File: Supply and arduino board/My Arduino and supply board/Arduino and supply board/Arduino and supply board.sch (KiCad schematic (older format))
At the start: 62 parts, among them J1 USB_C_Receptacle_USB2.0, J2 Conn_01x03, J3 Conn_01x03, J4 Conn_01x03, J5 Conn_01x03, J6 Conn_01x03, J7 Conn_01x03, Q2 16MHz, T1 FDN340V, U1 LM358D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

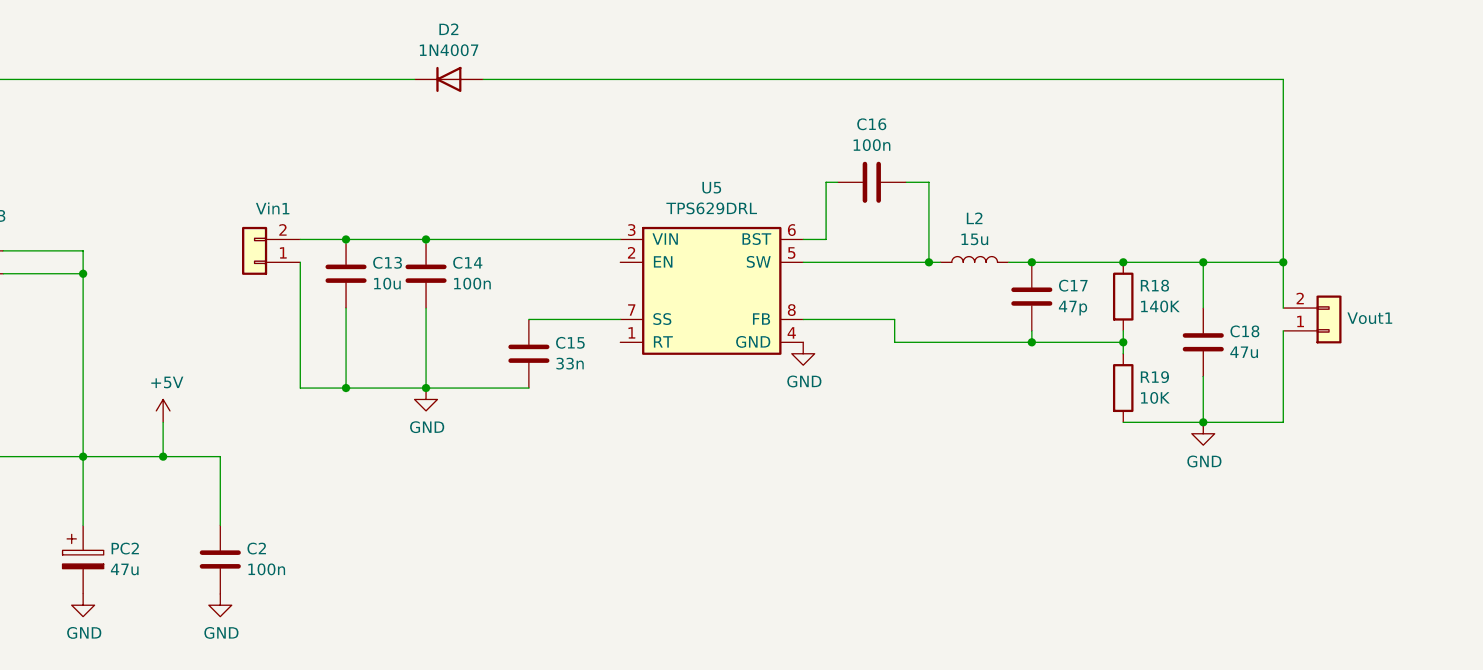
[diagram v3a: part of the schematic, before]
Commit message: new DC-DC power supply
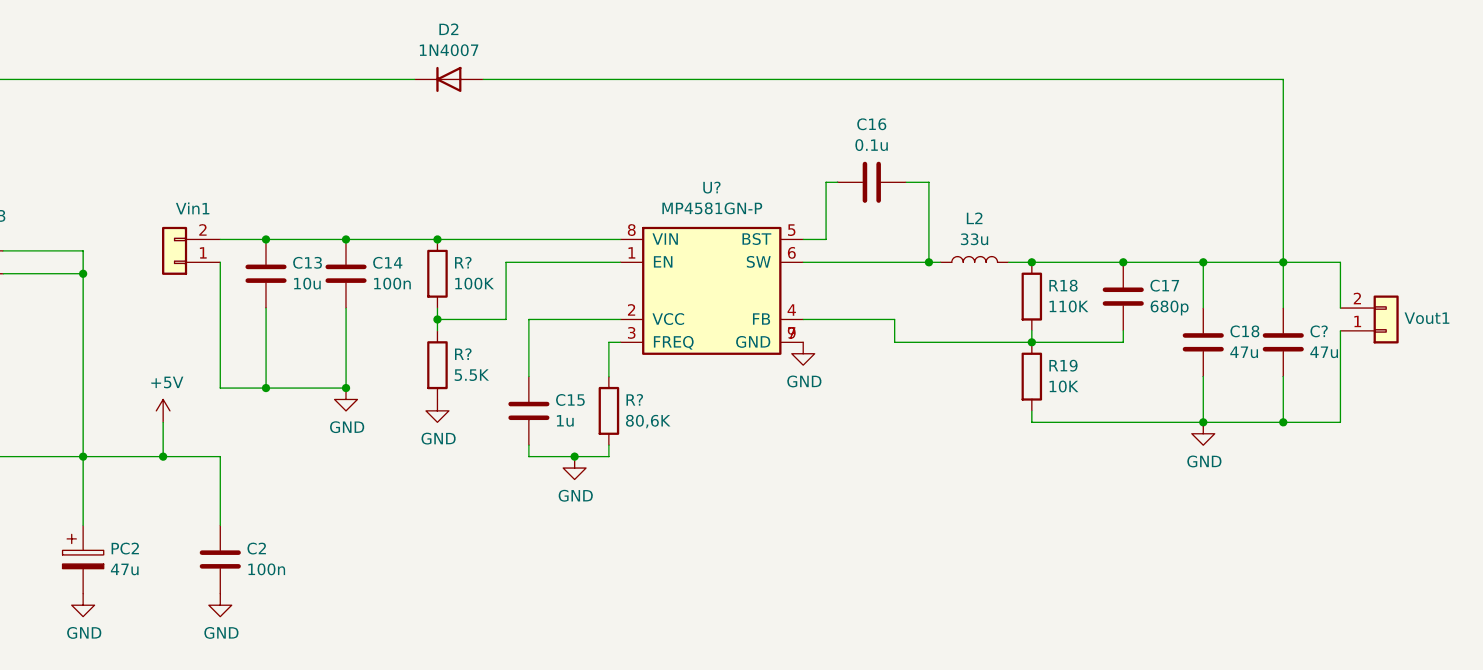
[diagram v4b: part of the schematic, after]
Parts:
- removed U5: TPS629DRL, Package_TO_SOT_SMD:TSOT-23-8, symbol Assembly_board_schem:TPS629DRL
- added C?: 47u, Capacitor_SMD:C_0603_1608Metric, symbol Device:C
- added R?: 100K, Resistor_SMD:R_0402_1005Metric, symbol Device:R
- added R?: 5.5K, Resistor_SMD:R_0402_1005Metric, symbol Device:R
- added R?: 80,6K, Resistor_SMD:R_0402_1005Metric, symbol Device:R
- added U?: MP4581GN-P, Package_SO:SOIC-8-1EP_3.9x4.9mm_P1.27mm_EP2.514x3.2mm, symbol Assembly_board_schem:MP4581GN-P
- C15: value 33n -> 1u
- C16: value 100n -> 0.1u
- C17: value 47p -> 680p
- L2: value 15u -> 33u
- R18: value 140K -> 110K
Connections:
- net GND: now also C?.1, R?.2, R?.2, U?.7 (GND), U?.9 (GND)
- net at C15.1: now also U?.2 (VCC)
- net at C13.1, C14.1, Vin1.2 (Pin_2): now also R?.1, U?.8 (VIN)
- net at C16.1, L2.1: now also U?.6 (SW)
- net at C16.2: now also U?.5 (BST)
- net at C17.1, R18.2, R19.1: now also U?.4 (FB)
- net at C17.2, C18.2, D2.2 (A)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: now also C?.2
- new net: R?.1, R?.2, U?.1 (EN)
- new net: R?.1, U?.3 (FREQ)
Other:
- moved on the sheet: C13, C14, C15, C17, R18, R19, Vin1, Vout1
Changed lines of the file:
@@
 L Device:C C15
 U 1 1 65724CD8
-P 12200 1850
-F 0 "C15" H 12315 1896 50  0000 L CNN
-F 1 "33n" H 12315 1805 50  0000 L CNN
-F 2 "Capacitor_SMD:C_0603_1608Metric" H 12238 1700 50  0001 C CNN
-F 3 "~" H 12200 1850 50  0001 C CNN
-	1    12200 1850
+P 12200 2100
+F 0 "C15" H 12315 2146 50  0000 L CNN
+F 1 "1u" H 12315 2055 50  0000 L CNN
+F 2 "Capacitor_SMD:C_0603_1608Metric" H 12238 1950 50  0001 C CNN
+F 3 "~" H 12200 2100 50  0001 C CNN
+	1    12200 2100
 	1    0    0    -1
 $EndComp
@@
 L Device:C C14
 U 1 1 6572633A
-P 11750 1500
-F 0 "C14" H 11865 1546 50  0000 L CNN
-F 1 "100n" H 11865 1455 50  0000 L CNN
-F 2 "Capacitor_SMD:C_0603_1608Metric" H 11788 1350 50  0001 C CNN
-F 3 "~" H 11750 1500 50  0001 C CNN
-	1    11750 1500
-	1    0    0    -1
-$EndComp
-$Comp
-L Device:C C13
-U 1 1 6572672D
 P 11400 1500
-F 0 "C13" H 11515 1546 50  0000 L CNN
-F 1 "10u" H 11515 1455 50  0000 L CNN
+F 0 "C14" H 11515 1546 50  0000 L CNN
+F 1 "100n" H 11515 1455 50  0000 L CNN
 F 2 "Capacitor_SMD:C_0603_1608Metric" H 11438 1350 50  0001 C CNN
 F 3 "~" H 11400 1500 50  0001 C CNN
@@
 $EndComp
 $Comp
+L Device:C C13
+U 1 1 6572672D
+P 11050 1500
+F 0 "C13" H 11165 1546 50  0000 L CNN
+F 1 "10u" H 11165 1455 50  0000 L CNN
+F 2 "Capacitor_SMD:C_0603_1608Metric" H 11088 1350 50  0001 C CNN
+F 3 "~" H 11050 1500 50  0001 C CNN
+	1    11050 1500
+	1    0    0    -1
+$EndComp
+$Comp
 L Connector_Generic:Conn_01x02 Vin1
 U 1 1 657270CA
-P 11000 1450
-F 0 "Vin1" H 10918 1217 50  0000 C CNN
-F 1 "Conn_01x02" H 10918 1216 50  0001 C CNN
-F 2 "Connector_PinSocket_2.54mm:PinSocket_1x02_P2.54mm_Horizontal" H 11000 1450 50  0001 C CNN
-F 3 "~" H 11000 1450 50  0001 C CNN
-	1    11000 1450
+P 10650 1450
+F 0 "Vin1" H 10568 1217 50  0000 C CNN
+F 1 "Conn_01x02" H 10568 1216 50  0001 C CNN
+F 2 "Connector_PinSocket_2.54mm:PinSocket_1x02_P2.54mm_Horizontal" H 10650 1450 50  0001 C CNN
+F 3 "~" H 10650 1450 50  0001 C CNN
+	1    10650 1450
 	-1   0    0    1
 $EndComp
@@
 P 13700 1100
 F 0 "C16" V 13448 1100 50  0000 C CNN
-F 1 "100n" V 13539 1100 50  0000 C CNN
+F 1 "0.1u" V 13539 1100 50  0000 C CNN
 F 2 "Capacitor_SMD:C_0603_1608Metric" H 13738 950 50  0001 C CNN
 F 3 "~" H 13700 1100 50  0001 C CNN
@@
 L Device:C C17
 U 1 1 657293B3
-P 14400 1600
-F 0 "C17" H 14285 1554 50  0000 R CNN
-F 1 "47p" H 14285 1645 50  0000 R CNN
-F 2 "Capacitor_SMD:C_0603_1608Metric" H 14438 1450 50  0001 C CNN
-F 3 "~" H 14400 1600 50  0001 C CNN
-	1    14400 1600
+P 14800 1600
+F 0 "C17" H 14685 1554 50  0000 R CNN
+F 1 "680p" H 14685 1645 50  0000 R CNN
+F 2 "Capacitor_SMD:C_0603_1608Metric" H 14838 1450 50  0001 C CNN
+F 3 "~" H 14800 1600 50  0001 C CNN
+	1    14800 1600
 	-1   0    0    1
 $EndComp
@@
 L Connector_Generic:Conn_01x02 Vout1
 U 1 1 65781F86
-P 15700 1750
-F 0 "Vout1" H 15780 1696 50  0000 L CNN
-F 1 "Conn_01x02" H 15780 1651 50  0001 L CNN
-F 2 "Connector_PinSocket_2.54mm:PinSocket_1x02_P2.54mm_Horizontal" H 15700 1750 50  0001 C CNN
-F 3 "~" H 15700 1750 50  0001 C CNN
-	1    15700 1750
+P 15950 1750
+F 0 "Vout1" H 16030 1696 50  0000 L CNN
+F 1 "Conn_01x02" H 16030 1651 50  0001 L CNN
+F 2 "Connector_PinSocket_2.54mm:PinSocket_1x02_P2.54mm_Horizontal" H 15950 1750 50  0001 C CNN
+F 3 "~" H 15950 1750 50  0001 C CNN
+	1    15950 1750
 	1    0    0    1
 $EndComp
 Wire Wire Line
-	11200 1350 11400 1350
+	10850 1350 11050 1350
+Connection ~ 11050 1350
+Wire Wire Line
+	11050 1350 11400 1350
 Connection ~ 11400 1350
 Wire Wire Line
-	11400 1350 11750 1350
-Connection ~ 11750 1350
-Wire Wire Line
-	11750 1350 12600 1350
-Wire Wire Line
-	11200 1450 11200 2000
-Wire Wire Line
-	11200 2000 11400 2000
-Wire Wire Line
-	12200 1700 12600 1700
-Wire Wire Line
-	11750 1650 11750 2000
-Connection ~ 11750 2000
-Wire Wire Line
-	11750 2000 12200 2000
+	10850 1450 10850 2000
+Wire Wire Line
+	10850 2000 11050 2000
 Wire Wire Line
 	11400 1650 11400 2000
 Connection ~ 11400 2000
 Wire Wire Line
-	11400 2000 11750 2000
+	11050 1650 11050 2000
+Connection ~ 11050 2000
+Wire Wire Line
+	11050 2000 11400 2000
 $Comp
 L power:GND #PWR0137
 U 1 1 65881DF1
-P 11750 2000
-F 0 "#PWR0137" H 11750 1750 50  0001 C CNN
-F 1 "GND" H 11755 1827 50  0000 C CNN
-F 2 "" H 11750 2000 50  0001 C CNN
-F 3 "" H 11750 2000 50  0001 C CNN
-	1    11750 2000
+P 11400 2000
+F 0 "#PWR0137" H 11400 1750 50  0001 C CNN
+F 1 "GND" H 11405 1827 50  0000 C CNN
+F 2 "" H 11400 2000 50  0001 C CNN
+F 3 "" H 11400 2000 50  0001 C CNN
+	1    11400 2000
 	1    0    0    -1
 $EndComp
@@
 P 14150 1450
 F 0 "L2" V 14340 1450 50  0000 C CNN
-F 1 "15u" V 14249 1450 50  0000 C CNN
+F 1 "33u" V 14249 1450 50  0000 C CNN
 F 2 "Inductor_SMD:L_Taiyo-Yuden_MD-5050" H 14150 1450 50  0001 C CNN
 F 3 "~" H 14150 1450 50  0001 C CNN
@@
 L Device:R R18
 U 1 1 658844CA
-P 14800 1600
-F 0 "R18" H 14870 1646 50  0000 L CNN
-F 1 "140K" H 14870 1555 50  0000 L CNN
-F 2 "Resistor_SMD:R_0402_1005Metric" V 14730 1600 50  0001 C CNN
-F 3 "~" H 14800 1600 50  0001 C CNN
-	1    14800 1600
+P 14400 1600
+F 0 "R18" H 14470 1646 50  0000 L CNN
+F 1 "110K" H 14470 1555 50  0000 L CNN
+F 2 "Resistor_SMD:R_0402_1005Metric" V 14330 1600 50  0001 C CNN
+F 3 "~" H 14400 1600 50  0001 C CNN
+	1    14400 1600
 	1    0    0    -1
 $EndComp
@@
 L Device:R R19
 U 1 1 658858B2
-P 14800 2000
-F 0 "R19" H 14870 2046 50  0000 L CNN
-F 1 "10K" H 14870 1955 50  0000 L CNN
-F 2 "Resistor_SMD:R_0402_1005Metric" V 14730 2000 50  0001 C CNN
-F 3 "~" H 14800 2000 50  0001 C CNN
-	1    14800 2000
+P 14400 1950
+F 0 "R19" H 14470 1996 50  0000 L CNN
+F 1 "10K" H 14470 1905 50  0000 L CNN
+F 2 "Resistor_SMD:R_0402_1005Metric" V 14330 1950 50  0001 C CNN
+F 3 "~" H 14400 1950 50  0001 C CNN
+	1    14400 1950
 	1    0    0    -1
 $EndComp
@@
 Wire Wire Line
 	14800 1450 15150 1450
-Wire Wire Line
-	15500 1450 15500 1650
 Connection ~ 14800 1450
 Wire Wire Line
@@
 Connection ~ 15150 2150
 Wire Wire Line
-	15150 2150 14800 2150
-Wire Wire Line
-	14800 1850 14800 1800
-Wire Wire Line
 	14800 1800 14400 1800
 Wire Wire Line
@@
 Wire Wire Line
 	13800 1700 13400 1700
-Connection ~ 14800 1800
 Wire Wire Line
 	14800 1800 14800 1750
@@
 F 3 "" H 9600 1500 50  0001 C CNN
 	1    9600 1500
-	1    0    0    -1
-$EndComp
-$Comp
-L Assembly_board_schem:TPS629DRL U5
-U 1 1 657CF2BB
-P 13000 1550
-F 0 "U5" H 13000 1975 50  0000 C CNN
-F 1 "TPS629DRL" H 13000 1884 50  0000 C CNN
-F 2 "Package_TO_SOT_SMD:TSOT-23-8" H 13000 1550 50  0001 C CNN
-F 3 "" H 13000 1550 50  0001 C CNN
-	1    13000 1550
 	1    0    0    -1
 $EndComp
@@
 Wire Wire Line
 	15500 650  12000 650
-Connection ~ 15500 1450
 Wire Wire Line
 	11700 650  8600 650
@@
 Wire Wire Line
 	8600 2300 8850 2300
-Wire Wire Line
-	15500 1750 15500 2150
+$Comp
+L Assembly_board_schem:MP4581GN-P U?
+U 1 1 658409AE
+P 13000 1550
+F 0 "U?" H 13000 1975 50  0000 C CNN
+F 1 "MP4581GN-P" H 13000 1884 50  0000 C CNN
+F 2 "Package_SO:SOIC-8-1EP_3.9x4.9mm_P1.27mm_EP2.514x3.2mm" H 13000 1550 50  0001 C CNN
+F 3 "" H 13000 1550 50  0001 C CNN
+	1    13000 1550
+	1    0    0    -1
+$EndComp
+$Comp
+L Device:R R?
+U 1 1 6582C206
+P 11800 1500
+F 0 "R?" H 11870 1546 50  0000 L CNN
+F 1 "100K" H 11870 1455 50  0000 L CNN
+F 2 "Resistor_SMD:R_0402_1005Metric" V 11730 1500 50  0001 C CNN
+F 3 "~" H 11800 1500 50  0001 C CNN
+	1    11800 1500
+	1    0    0    -1
+$EndComp
+$Comp
+L Device:R R?
+U 1 1 6582CDAE
+P 11800 1900
+F 0 "R?" H 11870 1946 50  0000 L CNN
+F 1 "5.5K" H 11870 1855 50  0000 L CNN
+F 2 "Resistor_SMD:R_0402_1005Metric" V 11730 1900 50  0001 C CNN
+F 3 "~" H 11800 1900 50  0001 C CNN
+	1    11800 1900
+	1    0    0    -1
+$EndComp
+Wire Wire Line
+	12100 1700 11800 1700
+Wire Wire Line
+	11800 1700 11800 1650
+Wire Wire Line
+	11800 1750 11800 1700
+Connection ~ 11800 1700
+Wire Wire Line
+	14400 2100 14400 2150
+Wire Wire Line
+	14400 2150 15150 2150
+Wire Wire Line
+	11400 1350 11800 1350
+Connection ~ 11800 1350
+Wire Wire Line
+	11800 1350 12600 1350
+Wire Wire Line
+	12100 1450 12100 1700
+Wire Wire Line
+	12100 1450 12600 1450
+$Comp
+L power:GND #PWR?
+U 1 1 658C02C0
+P 11800 2050
+F 0 "#PWR?" H 11800 1800 50  0001 C CNN
+F 1 "GND" H 11805 1877 50  0000 C CNN
+F 2 "" H 11800 2050 50  0001 C CNN
+F 3 "" H 11800 2050 50  0001 C CNN
+	1    11800 2050
+	1    0    0    -1
+$EndComp
+$Comp
+L Device:R R?
+U 1 1 658C089B
+P 12550 2100
+F 0 "R?" H 12620 2146 50  0000 L CNN
+F 1 "80,6K" H 12620 2055 50  0000 L CNN
+F 2 "Resistor_SMD:R_0402_1005Metric" V 12480 2100 50  0001 C CNN
+F 3 "~" H 12550 2100 50  0001 C CNN
+	1    12550 2100
+	1    0    0    -1
+$EndComp
+Wire Wire Line
+	12600 1800 12550 1800
+Wire Wire Line
+	12550 1800 12550 1950
+Wire Wire Line
+	12600 1700 12200 1700
+Wire Wire Line
+	12200 1700 12200 1950
+Wire Wire Line
+	12200 2250 12200 2300
+Wire Wire Line
+	12200 2300 12400 2300
+Wire Wire Line
+	12550 2300 12550 2250
+$Comp
+L power:GND #PWR?
+U 1 1 658FFE1C
+P 12400 2300
+F 0 "#PWR?" H 12400 2050 50  0001 C CNN
+F 1 "GND" H 12405 2127 50  0000 C CNN
+F 2 "" H 12400 2300 50  0001 C CNN
+F 3 "" H 12400 2300 50  0001 C CNN
+	1    12400 2300
+	1    0    0    -1
+$EndComp
+Connection ~ 12400 2300
+Wire Wire Line
+	12400 2300 12550 2300
+$Comp
+L Device:C C?
+U 1 1 659008EC
+P 15500 1800
+F 0 "C?" H 15385 1754 50  0000 R CNN
+F 1 "47u" H 15385 1845 50  0000 R CNN
+F 2 "Capacitor_SMD:C_0603_1608Metric" H 15538 1650 50  0001 C CNN
+F 3 "~" H 15500 1800 50  0001 C CNN
+	1    15500 1800
+	-1   0    0    1
+$EndComp
+Wire Wire Line
+	15500 1450 15500 1650
+Connection ~ 15500 1450
+Wire Wire Line
+	15500 1950 15500 2150
+Wire Wire Line
+	15750 1650 15750 1450
+Wire Wire Line
+	15750 1450 15500 1450
+Wire Wire Line
+	15750 1750 15750 2150
+Wire Wire Line
+	15750 2150 15500 2150
+Connection ~ 15500 2150
 $EndSCHEMATC

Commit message: change power supply 24v to 12v and 12v to 5v
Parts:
- removed PC1, PC2: 47u, Capacitor_SMD:CP_Elec_6.3x9.9, symbol Device:CP
- removed POWER1: Conn_01x06, Connector_PinHeader_2.54mm:PinHeader_1x06_P2.54mm_Vertical, symbol Connector_Generic:Conn_01x06
- removed T1: FDN340V, Package_TO_SOT_SMD:SOT-23, symbol Assembly_board_schem:FDN340V
- removed U1: LM358D, Package_SO:MSOP-8_3x3mm_P0.65mm, symbol Assembly_board_schem:LM358D
- removed U2: LP2985-3.3, Package_TO_SOT_SMD:SOT-23-5_HandSoldering, symbol Assembly_board_schem:LP2985-3.3
- removed U3: MC33269D-5.0, Package_TO_SOT_SMD:SOT-223-3_TabPin2, symbol Assembly_board_schem:MC33269D-5.0
- removed U4: MC33269ST-5.0T3, Package_TO_SOT_SMD:SOT-223, symbol Assembly_board_schem:MC33269ST-5.0T3
- added C11: 0.1u, Capacitor_SMD:C_0603_1608Metric, symbol Device:C
- added C19: 680p, Capacitor_SMD:C_0603_1608Metric, symbol Device:C
- added C20, C21: 47u, Capacitor_SMD:C_0603_1608Metric, symbol Device:C
- added J8: Programing_port, Connector_PinHeader_2.54mm:PinHeader_2x03_P2.54mm_Vertical, symbol Connector_Generic:Conn_02x03_Odd_Even
- added J9: Conn_01x05, Connector_PinHeader_2.54mm:PinHeader_1x05_P2.54mm_Vertical, symbol Connector_Generic:Conn_01x05
- added L1: 33u, Inductor_SMD:L_Wuerth_HCI-1040, symbol Device:L
- added R6: 82K, Resistor_SMD:R_0402_1005Metric, symbol Device:R
- added R7: 11K, Resistor_SMD:R_0402_1005Metric, symbol Device:R
- added R8: 43K, Resistor_SMD:R_0402_1005Metric, symbol Device:R
- added U1: MP4581GN-P, Package_SO:SOIC-8-1EP_3.9x4.9mm_P1.27mm_EP2.514x3.2mm, symbol Assembly_board_schem:MP4581GN-P
- added Vout2: +5V_out, Connector_Phoenix_MSTB:PhoenixContact_MSTBA_2,5_2-G-5,08_1x02_P5.08mm_Horizontal, symbol Connector_Generic:Conn_01x02
- C1: value 100n -> 10u
- L2: value 33u -> 47u; footprint Inductor_SMD:L_Taiyo-Yuden_MD-5050 -> Inductor_SMD:L_Wuerth_HCM-1350
- R15: renamed from R?; value 5.5K -> 5.6K
- R17: renamed from R?; value 80,6K -> 33K
- R4: value 10K -> 100K
- R5: value 10K -> 12K
- Vin1: value Conn_01x02 -> +24V_in; footprint Connector_PinSocket_2.54mm:PinSocket_1x02_P2.54mm_Horizontal -> Connector_Phoenix_MSTB:PhoenixContact_MSTBA_2,5_2-G-5,08_1x02_P5.08mm_Horizontal
- Vin2: value Conn_01x02 -> +12V_in; footprint Connector_PinSocket_2.54mm:PinSocket_1x02_P2.54mm_Horizontal -> Connector_Phoenix_MSTB:PhoenixContact_MSTBA_2,5_2-G-5,08_1x02_P5.08mm_Horizontal
- Vout1: value Conn_01x02 -> +12V_out; footprint Connector_PinSocket_2.54mm:PinSocket_1x02_P2.54mm_Horizontal -> Connector_Phoenix_MSTB:PhoenixContact_MSTBA_2,5_2-G-5,08_1x02_P5.08mm_Horizontal
- gave numbers to parts that had none: 3
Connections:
- net +3V3 is gone; now on net GND: C3.2
- net +5V: now also C19.2, C20.2, C21.2, J8.2 (Pin_2), J9.2 (Pin_2), L1.2, R7.1, Vout2.2 (Pin_2); no longer C1.2, C2.1
- net GND: now also C1.2, R5.2, C20.1, C21.1, J8.6 (Pin_6), J9.3 (Pin_3), J9.4 (Pin_4), R6.2, R8.2, U1.7 (GND), U1.9 (GND), Vout2.1 (Pin_1); no longer C1.1, C3.1, R5.1
- net RESET: now also J8.5 (Pin_5), J9.1 (Pin_1)
- net VIN+24V: now reaches C13.1, C14.1, R14.1, U2.8 (VIN), Vin1.2 (Pin_2)
- net VOUT+12V: now reaches C17.2, C18.2, C22.2, D2.2 (A), L2.2, R18.1, Vout1.2 (Pin_2)
- net MOSI: now reaches U7.17 (PB3)
- net MOSI: now also J8.4 (Pin_4)
- net MISO: now reaches U7.18 (PB4)
- net MISO: now also J8.1 (Pin_1)
- net SCK: now reaches U7.19 (PB5)
- net SCK: now also J8.3 (Pin_3)
- net CMP renamed VIN+12V
- net VIN+12V: now also C1.1, C2.1, D1.1 (K), D2.1 (K), J9.5 (Pin_5), U1.8 (VIN); no longer R5.2
- net PWRIM: no longer names the net of D1.2 (A), Vin2.2 (Pin_2)
- removed net VIN: D1.1 (K), D2.1 (K), R4.2
- new net: C3.1, U1.2 (VCC)
- new net: C11.1, L1.1, U1.6 (SW)
- new net: C11.2, U1.5 (BST)
- new net: C19.1, R7.2, R8.1, U1.4 (FB)
- new net: R4.2, R5.1, U1.1 (EN)
- new net: R6.1, U1.3 (FREQ)
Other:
- moved on the sheet: C13, C14, C15, C16, C17, C18, C22, D1, D2, L2, R14, R15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
